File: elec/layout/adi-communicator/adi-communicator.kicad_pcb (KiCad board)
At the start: 2 copper layers, 225.7 x 100.8 mm, 0 parts

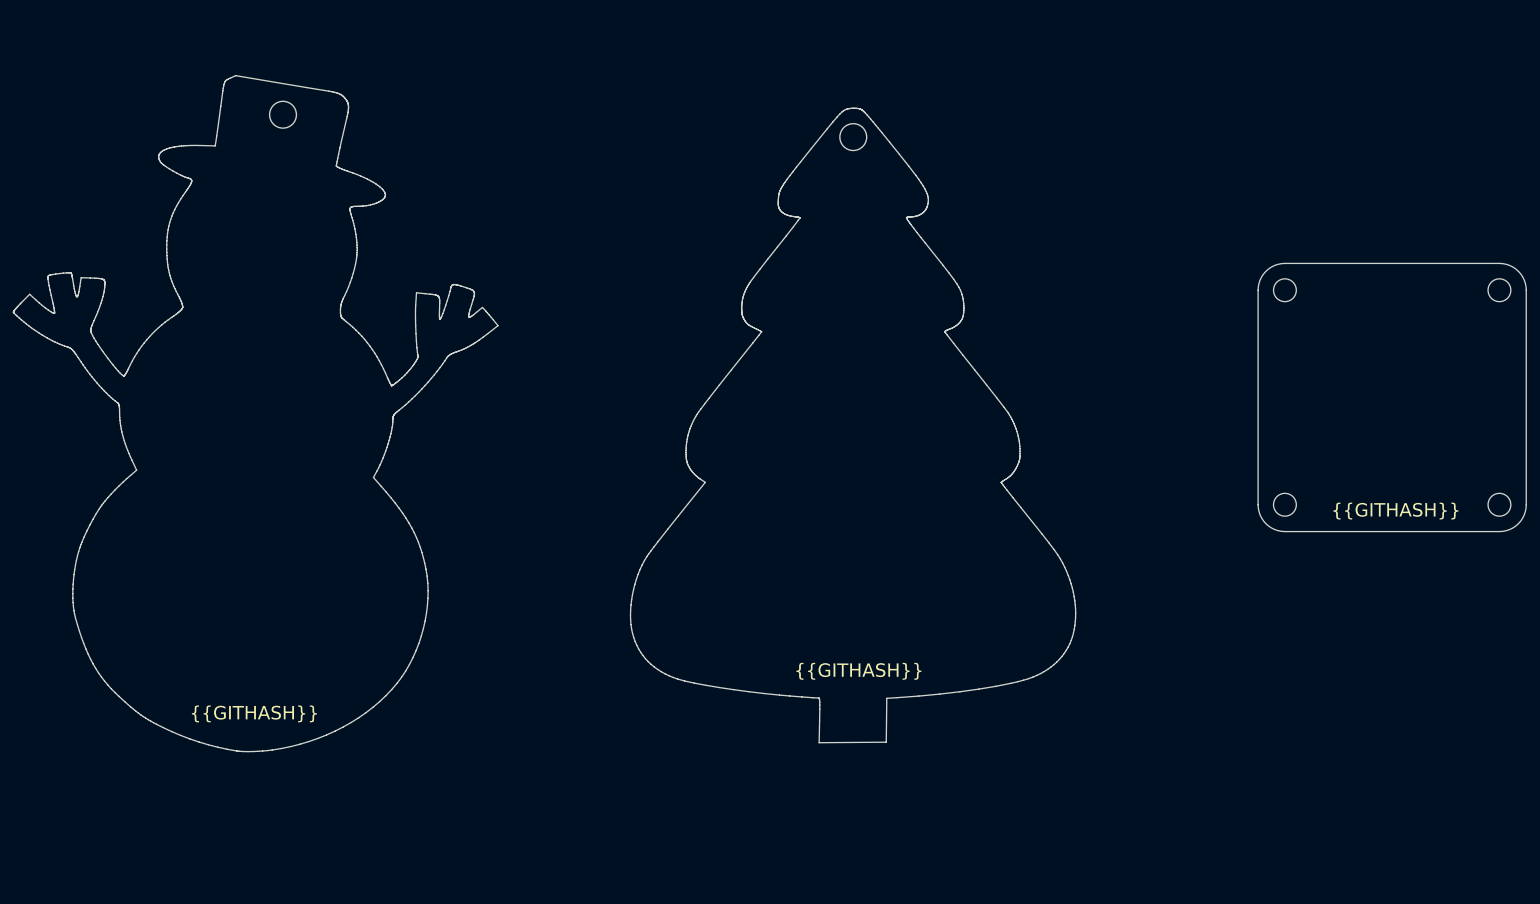
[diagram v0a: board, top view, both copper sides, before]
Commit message: Remove xmas tree from layout
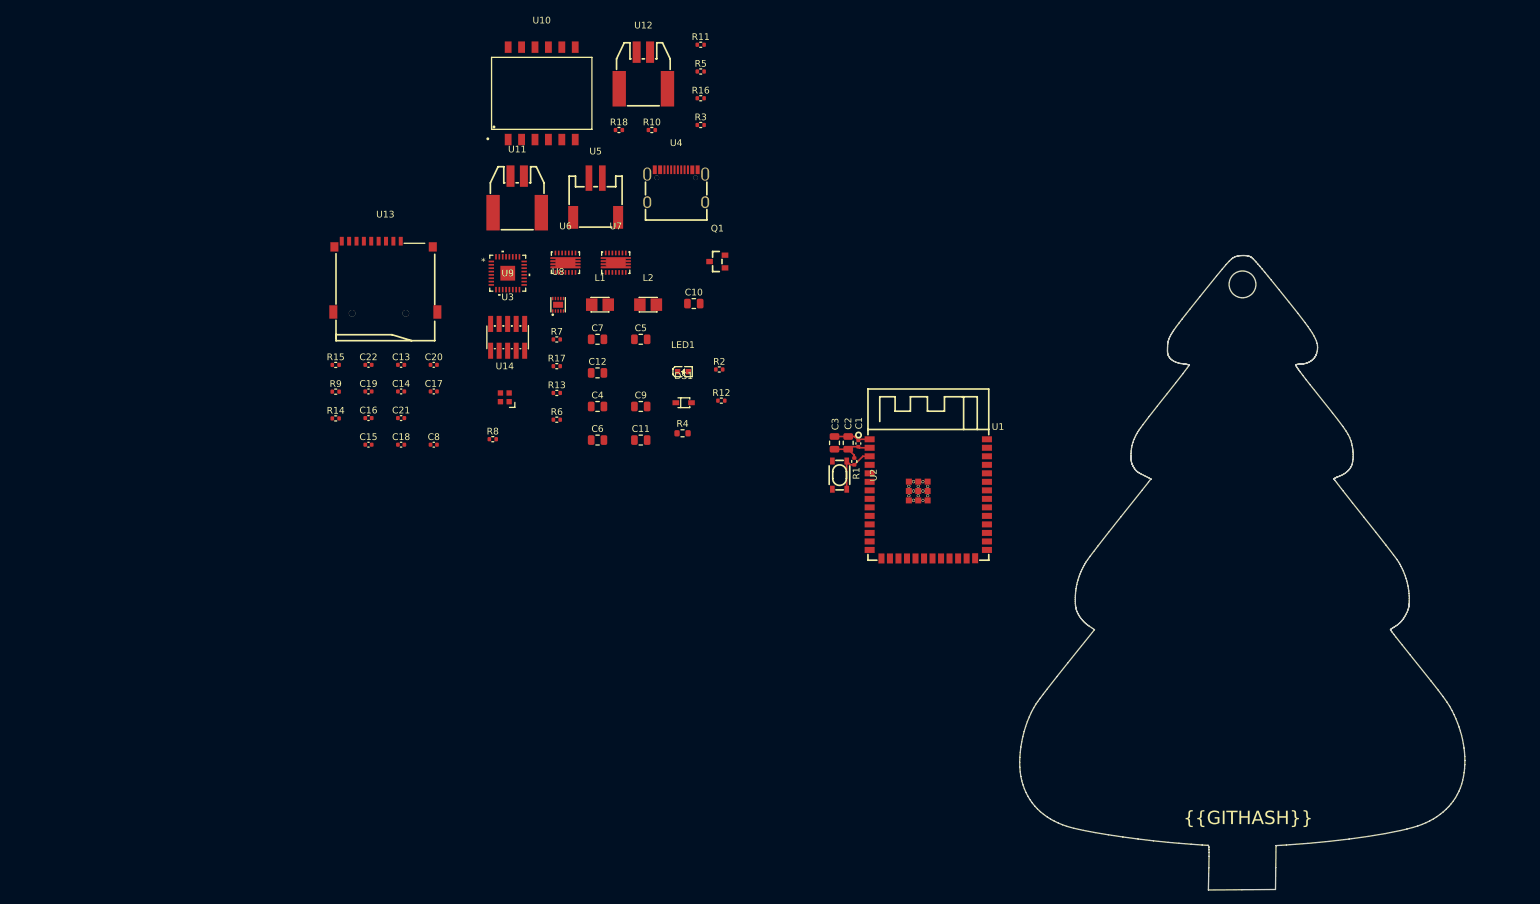
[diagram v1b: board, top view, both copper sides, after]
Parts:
- added C1: 16V 100nF X7R ±10% 0402 Multilayer Ceramic Capacitors MLCC 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, lib:C0402, F.Cu at (162.0, 104.7)
- added C10: 25V 10uF X5R ±10% 0805 Multilayer Ceramic Capacitors MLCC -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, lib:C0805, F.Cu at (137.4, 83.8)
- added C11: 25V 10uF X5R ±10% 0805 Multilayer Ceramic Capacitors MLCC -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, lib:C0805, F.Cu at (129.5, 104.1)
- added C12: 25V 10uF X5R ±10% 0805 Multilayer Ceramic Capacitors MLCC -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, lib:C0805, F.Cu at (123.1, 94.1)
- added C13: 16V 100nF X7R ±10% 0402 Multilayer Ceramic Capacitors MLCC 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, lib:C0402, F.Cu at (93.8, 92.9)
- added C14: 25V 1uF X5R ±10% 0402 Multilayer Ceramic Capacitors MLCC - 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, lib:C0402, F.Cu at (93.8, 96.9)
- added C15: 25V 1uF X5R ±10% 0402 Multilayer Ceramic Capacitors MLCC - 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, lib:C0402, F.Cu at (88.9, 104.8)
- added C16: 16V 100nF X7R ±10% 0402 Multilayer Ceramic Capacitors MLCC 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, lib:C0402, F.Cu at (88.9, 100.9)
- added C17: 16V 100nF X7R ±10% 0402 Multilayer Ceramic Capacitors MLCC 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, lib:C0402, F.Cu at (98.7, 96.9)
- added C18: 16V 100nF X7R ±10% 0402 Multilayer Ceramic Capacitors MLCC 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, lib:C0402, F.Cu at (93.8, 104.8)
- added C19: 16V 100nF X7R ±10% 0402 Multilayer Ceramic Capacitors MLCC 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, lib:C0402, F.Cu at (88.9, 96.9)
- added C2: 25V 10uF X5R ±10% 0805 Multilayer Ceramic Capacitors MLCC -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, lib:C0805, F.Cu at (160.5, 104.6)
- added C20: 16V 100nF X7R ±10% 0402 Multilayer Ceramic Capacitors MLCC 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, lib:C0402, F.Cu at (98.7, 92.9)
- added C21: 16V 100nF X7R ±10% 0402 Multilayer Ceramic Capacitors MLCC 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, lib:C0402, F.Cu at (93.8, 100.9)
- added C22: 16V 100nF X7R ±10% 0402 Multilayer Ceramic Capacitors MLCC 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, lib:C0402, F.Cu at (88.9, 92.9)
- added C3: 25V 10uF X5R ±10% 0805 Multilayer Ceramic Capacitors MLCC -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, lib:C0805, F.Cu at (158.4, 104.6)
- added C4: 25V 10uF X5R ±10% 0805 Multilayer Ceramic Capacitors MLCC -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, lib:C0805, F.Cu at (123.1, 99.1)
- added C5: 25V 10uF X5R ±10% 0805 Multilayer Ceramic Capacitors MLCC -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, lib:C0805, F.Cu at (129.5, 89.1)
- added C6: 25V 10uF X5R ±10% 0805 Multilayer Ceramic Capacitors MLCC -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, lib:C0805, F.Cu at (123.1, 104.1)
- added C7: 25V 10uF X5R ±10% 0805 Multilayer Ceramic Capacitors MLCC -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, lib:C0805, F.Cu at (123.1, 89.1)
- added C8: 16V 100nF X7R ±10% 0402 Multilayer Ceramic Capacitors MLCC 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, lib:C0402, F.Cu at (98.7, 104.8)
- added C9: 25V 10uF X5R ±10% 0805 Multilayer Ceramic Capacitors MLCC -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, lib:C0805, F.Cu at (129.5, 99.1)
- added DS1: , lib:SOD-323_L1.8-W1.3-LS2.5-RD, F.Cu at (135.9, 98.6)
- added L1: , lib:IND-SMD_L2.5-W2.0_WPN252012H, F.Cu at (123.4, 83.9)
- added L2: , lib:IND-SMD_L2.5-W2.0_WPN252012H, F.Cu at (130.6, 83.9)
- added LED1: , lib:LED0603-RD, F.Cu at (135.8, 93.9)
- added Q1: , lib:SOT-23_L2.9-W1.3-P1.90-LS2.4-BR, F.Cu at (140.9, 77.5)
- added R1: 62.5mW Thick Film Resistors 50V ±100ppm/℃ ±1% 10kΩ 0402 Chi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, lib:R0402, F.Cu at (161.4, 107.3)
- added R10: 62.5mW Thick Film Resistors 50V ±100ppm/℃ ±1% 1MΩ 0402 Chip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, lib:R0402, F.Cu at (131.2, 57.9)
- added R11: 62.5mW Thick Film Resistors 50V ±100ppm/℃ ±1% 330Ω 0402 Chi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, lib:R0402, F.Cu at (138.5, 45.2)
- added R12: 62.5mW Thick Film Resistors 75V ±1% ±100ppm/℃ 576Ω 0402 Chi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, lib:R0402, F.Cu at (141.6, 98.3)
- added R13: 0Ω, lib:R0402, F.Cu at (117.0, 97.1)
- added R14: 0Ω, lib:R0402, F.Cu at (84.0, 100.9)
- added R15: 0Ω, lib:R0402, F.Cu at (84.0, 92.9)
- added R16: 0Ω, lib:R0402, F.Cu at (138.5, 53.1)
- added R17: 0Ω, lib:R0402, F.Cu at (117.0, 93.1)
- added R18: 0Ω, lib:R0402, F.Cu at (126.3, 57.9)
- added R2: 62.5mW Thick Film Resistors 50V ±100ppm/℃ ±1% 4.7kΩ 0402 Ch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, lib:R0402, F.Cu at (141.2, 93.6)
- added R3: 62.5mW Thick Film Resistors 50V ±100ppm/℃ ±1% 4.7kΩ 0402 Ch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, lib:R0402, F.Cu at (138.5, 57.1)
- added R4: 100mW Thick Film Resistors 75V ±100ppm/℃ ±1% 10kΩ 0603 Chip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, lib:R0603, F.Cu at (135.8, 103.1)
- added R5: 62.5mW Thick Film Resistors 50V ±100ppm/℃ ±1% 25.5kΩ 0402 C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, lib:R0402, F.Cu at (138.5, 49.2)
- added R6: 62.5mW Thick Film Resistors ±100ppm/℃ ±1% 2.8kΩ 0402 Chip R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, lib:R0402, F.Cu at (117.0, 101.1)
- added R7: 62.5mW Thick Film Resistors 50V ±100ppm/℃ ±1% 1MΩ 0402 Chip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, lib:R0402, F.Cu at (117.0, 89.1)
- added R8: 62.5mW Thick Film Resistors 50V ±100ppm/℃ ±1% 23.7kΩ 0402 C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, lib:R0402, F.Cu at (107.5, 104.0)
- added R9: 62.5mW Thick Film Resistors 50V ±100ppm/℃ ±1% 4.3kΩ 0402 Ch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, lib:R0402, F.Cu at (84.0, 96.9)
- added U1: , lib:WIRELM-SMD_ESP32-S3-WROOM-1, F.Cu at (172.4, 112.9)
- added U10: , lib:SMD-12_L14.8-W11.7-P2.00-LS14.7, F.Cu at (114.8, 52.4)
- added U11: , lib:CONN-SMD_2P-P2.00_MOLEX_5023520201, F.Cu at (111.1, 67.5)
- added U12: , lib:CONN-SMD_2P-P2.00_MOLEX_5023520201, F.Cu at (129.9, 49.0)
- added U13: , lib:TF-SMD_TF-01A, F.Cu at (91.4, 79.8)
- added U14: , lib:LED-SMD_4P-L2.0-W2.0-BR, F.Cu at (109.2, 97.8)
- added U2: , lib:KEY-SMD_4P-L4.2-W3.2-P2.20-LS4.6, F.Cu at (159.2, 109.4)
- added U3: , lib:HDR-SMD_10P-P1.27-V-M-R2-C5-LS5.3, F.Cu at (109.7, 88.8)
- added U4: , lib:USB-C-SMD_KH-TYPE-C-16P, F.Cu at (134.8, 66.2)
- added U5: , lib:CONN-SMD_P2.00_S2B-PH-SM4-TB-LF-SN, F.Cu at (122.8, 68.0)
- added U6: , lib:VSON-14_L4.0-W3.0-P0.50-BL-EP_TI_DSJ, F.Cu at (118.3, 77.7)
- added U7: , lib:VSON-14_L4.0-W3.0-P0.50-BL-EP_TI_DSJ, F.Cu at (125.8, 77.7)
- added U8: , lib:WSON-10_L2.0-W2.0-P0.40-BL-EP, F.Cu at (117.2, 84.0)
- added U9: , lib:05-08-7057_ADI, F.Cu at (109.7, 79.3)
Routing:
- net en: track 0.00 -> 8.40 mm
- net uc.ic-vcc: track 0.00 -> 7.15 mm
- net uc.ic-gnd: track 0.00 -> 5.54 mm
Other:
- board size 225.7 x 100.8 mm -> 66.4 x 94.6 mm

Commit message: Placement and zones done. Small routing largely complete
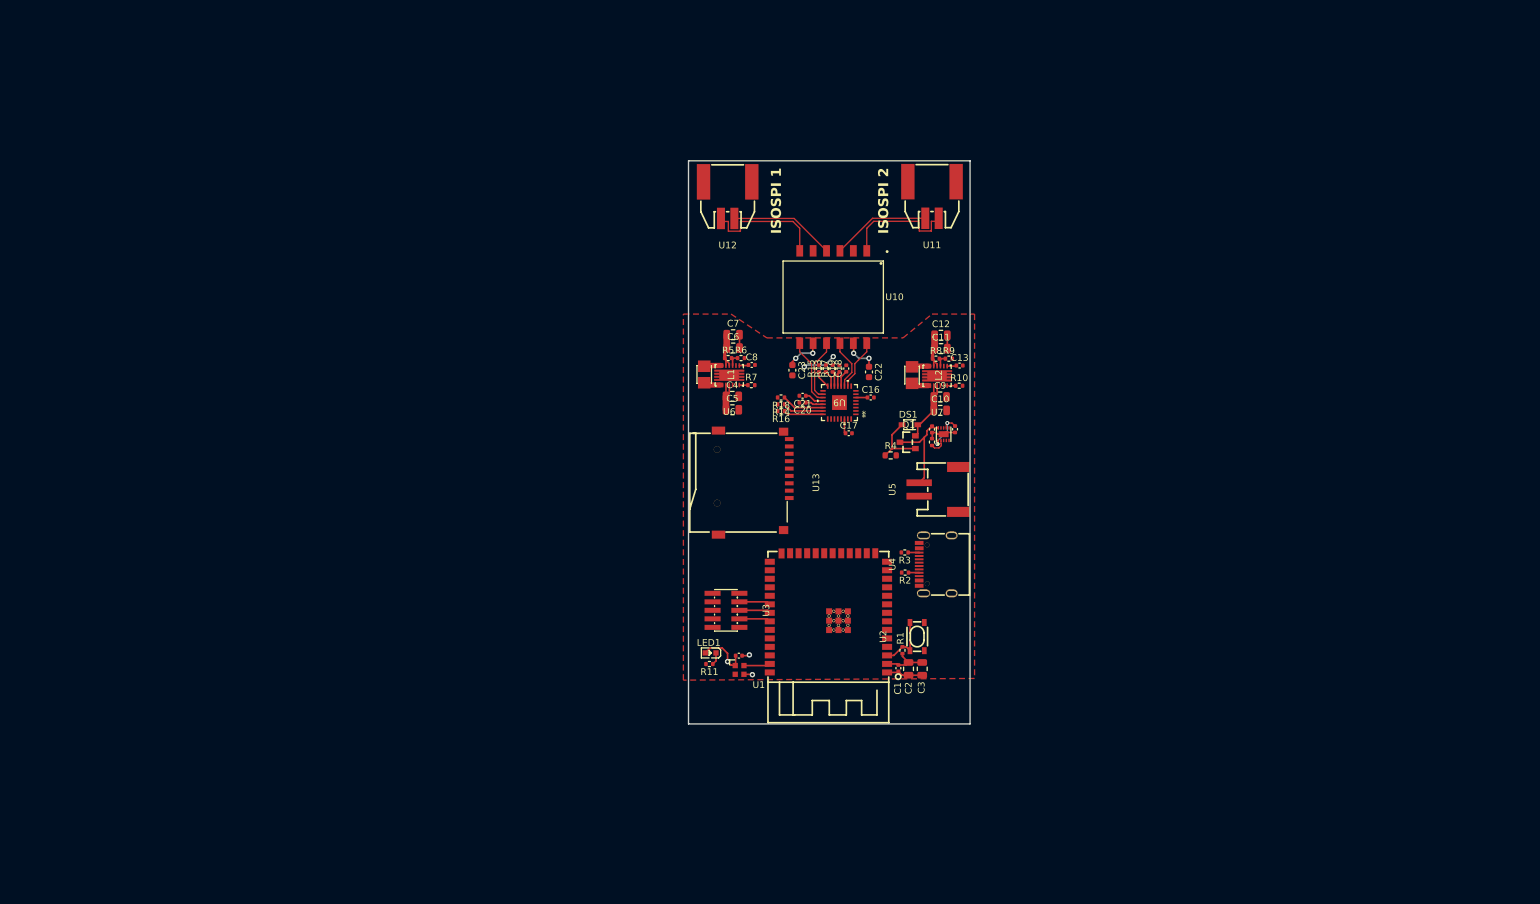
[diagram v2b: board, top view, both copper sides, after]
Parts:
- added C22: 50V 10nF X7R ±10% 0603 Multilayer Ceramic Capacitors MLCC -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, lib:C0603, F.Cu at (163.6, 94.0)
- added C23: 50V 10nF X7R ±10% 0603 Multilayer Ceramic Capacitors MLCC -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, lib:C0603, F.Cu at (152.1, 93.7)
- moved R11 92.4 mm to (139.8, 137.5), turned to 180 degrees
- moved R9 91.6 mm to (175.5, 92.0)
- moved C15 84.1 mm to (173.0, 102.5), turned to -90 degrees
- moved C13 83.3 mm to (177.1, 93.0)
- moved C14 82.8 mm to (176.4, 102.5), turned to -90 degrees
- moved C16 75.0 mm to (163.8, 97.8)
- moved R15 72.1 mm to (156.1, 93.5), turned to 90 degrees
- moved R3 70.7 mm to (168.9, 120.9), turned to 180 degrees
- moved C19 70.3 mm to (159.2, 93.5), turned to 90 degrees
- moved C24 70.2 mm to (144.2, 136.3)
- moved U4 68.4 mm to (173.5, 122.7), turned to 90 degrees
- moved C18 67.4 mm to (160.2, 93.5), turned to 90 degrees
- moved R8 67.2 mm to (173.6, 92.0)
- moved U5 67.2 mm to (174.0, 111.5), turned to 90 degrees
- moved R14 66.5 mm to (150.5, 98.8), turned to 180 degrees
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- renumbered C22 to C24
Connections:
- C10 pad 2: uc-gnd-1 -> uc.ic-gnd
- C11 pad 1: _3v3_reg-vcc -> uc.ic-vcc
- C11 pad 2: uc-gnd-1 -> uc.ic-gnd
- C12 pad 1: _3v3_reg-vcc -> uc.ic-vcc
- C12 pad 2: uc-gnd-1 -> uc.ic-gnd
- C13 pad 2: uc-gnd-1 -> uc.ic-gnd
- C14 pad 2: uc-gnd-1 -> uc.ic-gnd
- C15 pad 2: uc-gnd-1 -> uc.ic-gnd
- C16 pad 1: _nic._ic-vcc -> uc.ic-vcc
- C16 pad 2: _nic-gnd -> uc.ic-gnd
- C17 pad 1: _nic._ic-vcc -> uc.ic-vcc
- C17 pad 2: _nic-gnd -> uc.ic-gnd
- C18 pad 1: _nic._ic-vcc -> _5v_reg-vcc
- C18 pad 2: _nic-gnd -> uc.ic-gnd
- C19 pad 1: _nic._ic-vcc -> _5v_reg-vcc
- C19 pad 2: _nic-gnd -> uc.ic-gnd
- C20 pad 1: _nic._ic-vcc -> _5v_reg-vcc
- C20 pad 2: _nic-gnd -> uc.ic-gnd
- C21 pad 1: _nic._ic-vcc -> _5v_reg-vcc
- C21 pad 2: _nic-gnd -> uc.ic-gnd
- C24 pad 1: _led.ic-vcc -> uc.ic-vcc
- C24 pad 2: _led.ic-gnd -> uc.ic-gnd
- C4 pad 2: uc-gnd-1 -> uc.ic-gnd
- C5 pad 2: uc-gnd-1 -> uc.ic-gnd
- C6 pad 2: uc-gnd-1 -> uc.ic-gnd
- C7 pad 2: uc-gnd-1 -> uc.ic-gnd
- C8 pad 2: uc-gnd-1 -> uc.ic-gnd
- C9 pad 2: uc-gnd-1 -> uc.ic-gnd
- LED1 pad 2: _3v3_reg-vcc -> uc.ic-vcc
- R10 pad 2: uc-gnd-1 -> uc.ic-gnd
- R11 pad 2: uc-gnd-1 -> uc.ic-gnd
- R12 pad 2: uc-gnd-1 -> uc.ic-gnd
- R13 pad 2: _nic-gnd -> uc.ic-gnd
- R14 pad 2: _nic-gnd -> uc.ic-gnd
- R15 pad 1: rto -> xcvrmd
- R15 pad 2: _nic-gnd -> uc.ic-gnd
- R16 pad 1: rto2 -> xcvrmd2
- R16 pad 2: _nic-gnd -> uc.ic-gnd
- R17 pad 1: rto -> phapol
- R17 pad 2: _nic-gnd -> uc.ic-gnd
- R18 pad 1: rto2 -> phapol2
- R18 pad 2: _nic-gnd -> uc.ic-gnd
- R2 pad 2: uc-gnd-1 -> uc.ic-gnd
- R3 pad 2: uc-gnd-1 -> uc.ic-gnd
- R4 pad 2: uc-gnd-1 -> uc.ic-gnd
- R6 pad 2: uc-gnd-1 -> uc.ic-gnd
- R7 pad 2: uc-gnd-1 -> uc.ic-gnd
- R8 pad 1: _3v3_reg-vcc -> uc.ic-vcc
- R9 pad 2: uc-gnd-1 -> uc.ic-gnd
- U1 pad 15: io3 -> uc.ic-sck-1
- U1 pad 16: io46 -> uc.ic-miso-1
- U1 pad 17: io9 -> uc.ic-mosi-1
- U1 pad 19: uc.ic-mosi-1 -> uc.ic-mosi
- U1 pad 20: uc.ic-sck-1 -> uc.ic-sck
- U1 pad 21: uc.ic-miso-1 -> uc.ic-miso
- U1 pad 28: uc.ic-miso -> io35
- U1 pad 29: uc.ic-mosi -> io36
- U1 pad 30: uc.ic-sck -> io37
- U10 pad 1: _iso_transformer-p -> isospi_hv_1-
- U10 pad 10: _nic._ic-n -> isospi_safe_1+
- U10 pad 12: _nic._ic-p -> isospi_safe_1-
- U10 pad 3: _iso_transformer-n -> isospi_hv_1+
- U10 pad 4: _iso_transformer-p-1 -> isospi_hv_2-
- U10 pad 6: _iso_transformer-n-1 -> isospi_hv_2+
- U10 pad 7: _nic._ic-n-1 -> isospi_safe_2+
- U10 pad 9: _nic._ic-p-1 -> isospi_safe_2-
- U11 pad 1: _iso_transformer-p -> isospi_hv_1+
- U11 pad 2: _iso_transformer-n -> isospi_hv_1-
- U12 pad 1: _iso_transformer-p-1 -> isospi_hv_2+
- U12 pad 2: _iso_transformer-n-1 -> isospi_hv_2-
- U13 pad 10: uc-gnd-1 -> uc.ic-gnd
- U13 pad 11: uc-gnd-1 -> uc.ic-gnd
- U13 pad 12: uc-gnd-1 -> uc.ic-gnd
- U13 pad 13: uc-gnd-1 -> uc.ic-gnd
- U13 pad 3: uc.ic-mosi-1 -> uc.ic-mosi
- U13 pad 4: _3v3_reg-vcc -> uc.ic-vcc
- U13 pad 5: uc.ic-sck-1 -> uc.ic-sck
- U13 pad 6: uc-gnd-1 -> uc.ic-gnd
- U13 pad 7: uc.ic-miso-1 -> uc.ic-miso
- U14 pad 1: _led.ic-vcc -> uc.ic-vcc
- U14 pad 2: _led.ic-vcc-1 -> _led.ic-vcc
- U14 pad 3: _led.ic-gnd -> uc.ic-gnd
- U14 pad 4: io21 -> io1
- U4 pad 1: uc-gnd-1 -> uc.ic-gnd
- U4 pad 2: uc-gnd-1 -> uc.ic-gnd
- U4 pad 3: uc-gnd-1 -> uc.ic-gnd
- U4 pad 4: uc-gnd-1 -> uc.ic-gnd
- U4 pad A1: uc-gnd-1 -> uc.ic-gnd
- U4 pad A12: uc-gnd-1 -> uc.ic-gnd
- U4 pad B1: uc-gnd-1 -> uc.ic-gnd
- U4 pad B12: uc-gnd-1 -> uc.ic-gnd
- U5 pad 1: uc-gnd-1 -> uc.ic-gnd
- U6 pad 13: uc-gnd-1 -> uc.ic-gnd
- U6 pad 15: uc-gnd-1 -> uc.ic-gnd
- U6 pad 2: uc-gnd-1 -> uc.ic-gnd
- U7 pad 13: uc-gnd-1 -> uc.ic-gnd
- U7 pad 15: uc-gnd-1 -> uc.ic-gnd
- U7 pad 2: uc-gnd-1 -> uc.ic-gnd
- U7 pad 4: _3v3_reg-vcc -> uc.ic-vcc
- U7 pad 5: _3v3_reg-vcc -> uc.ic-vcc
- U8 pad 11: uc-gnd-1 -> uc.ic-gnd
- U8 pad 3: uc-gnd-1 -> uc.ic-gnd
- U9 pad 10: _nic._ic-n -> isospi_safe_1-
- U9 pad 11: _nic._ic-p -> isospi_safe_1+
- U9 pad 12: vdd -> _5v_reg-vcc
- U9 pad 13: vdd -> _5v_reg-vcc
- U9 pad 17: _nic-gnd -> uc.ic-gnd
- U9 pad 18: _nic._ic-n-1 -> isospi_safe_2-
- U9 pad 19: _nic._ic-p-1 -> isospi_safe_2+
- U9 pad 2: uc.ic-mosi -> uc.ic-mosi-1
- U9 pad 20: vdd -> _5v_reg-vcc
- U9 pad 21: vdd -> _5v_reg-vcc
- U9 pad 26: uc.ic-mosi -> uc.ic-mosi-1
- U9 pad 27: uc.ic-miso -> uc.ic-miso-1
- U9 pad 28: uc.ic-sck -> uc.ic-sck-1
- U9 pad 29: io45 -> io18
- U9 pad 3: uc.ic-miso -> uc.ic-miso-1
- U9 pad 30: _nic._ic-vcc -> uc.ic-vcc
- U9 pad 33: _nic-gnd -> uc.ic-gnd
- U9 pad 4: uc.ic-sck -> uc.ic-sck-1
- U9 pad 5: io38 -> io8
- U9 pad 6: _nic._ic-vcc -> uc.ic-vcc
- U9 pad 9: _nic-gnd -> uc.ic-gnd
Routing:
- net isospi_hv_2+: track 0.00 -> 18.6 mm
- net uc.ic-vcc: track 7.15 -> 25.4 mm, vias 0 -> 1
- net isospi_hv_1-: track 0.00 -> 17.6 mm
- net _5v_reg-vcc: track 0.00 -> 16.5 mm
- net power_prio-vcc: track 0.00 -> 16.4 mm
- net uc.ic-gnd: track 5.54 -> 21.4 mm, vias 0 -> 4
- net isospi_hv_2-: track 0.00 -> 15.8 mm
- net usb_conn-vcc: track 0.00 -> 15.6 mm, vias 0 -> 2
- net isospi_hv_1+: track 0.00 -> 14.7 mm
- net battery_conn-vcc: track 0.00 -> 14.3 mm
- net isospi_safe_2+: track 0.00 -> 10.0 mm
- net isospi_safe_2-: track 0.00 -> 9.32 mm
- net isospi_safe_1-: track 0.00 -> 7.60 mm
- net isospi_safe_1+: track 0.00 -> 7.59 mm
- net phapol2: track 0.00 -> 6.38 mm
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- added copper zone on F.Cu, net uc.ic-gnd
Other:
- board size 66.4 x 94.6 mm -> 42 x 84 mm
- copper layers 2 -> 4
- board text added: "ISOSPI 1"
- board text added: "ISOSPI 2"
- board text removed: "{{GITHASH}}"

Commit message: Layout communicator
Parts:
- added REF**: MountingHole_3.2mm_M3_DIN965_Pad, MountingHole:MountingHole_3.2mm_M3_DIN965_Pad, F.Cu at (158.2, 67.1)
- added REF**: MountingHole_3.2mm_M3_DIN965_Pad, MountingHole:MountingHole_3.2mm_M3_DIN965_Pad, F.Cu at (140.0, 143.0)
- added REF**: MountingHole_3.2mm_M3_DIN965_Pad, MountingHole:MountingHole_3.2mm_M3_DIN965_Pad, F.Cu at (175.3, 143.0)
- added REF**: PinHeader_1x04_P2.54mm_Vertical, Connector_PinHeader_2.54mm:PinHeader_1x04_P2.54mm_Vertical, F.Cu at (138.4, 122.2)
- added REF**: PinHeader_1x04_P2.54mm_Vertical, Connector_PinHeader_2.54mm:PinHeader_1x04_P2.54mm_Vertical, B.Cu at (176.0, 137.4)
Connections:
- net dm renamed usb-
- net dp renamed usb+
- U9 pad 29: io18 -> io8
- U9 pad 5: io8 -> io18
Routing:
- net uc.ic-sck-1: track 0.00 -> 35.6 mm, vias 0 -> 2
- net uc.ic-miso-1: track 0.00 -> 35.6 mm, vias 0 -> 2
- net usb_conn-vcc: track 15.6 -> 51.1 mm, vias 2 -> 4
- net io18: track 0.00 -> 34.7 mm, vias 0 -> 2
- net power_prio-vcc: track 16.4 -> 47.7 mm, vias 0 -> 2
- net io8: track 0.00 -> 30.2 mm, vias 0 -> 2
- net uc.ic-mosi-1: track 0.00 -> 26.3 mm
- net _5v_reg-vcc: track 16.5 -> 38.3 mm
- net uc.ic-miso: track 0.00 -> 19.8 mm
- net uc.ic-gnd: track 21.4 -> 40.9 mm, vias 4 -> 11
- net uc.ic-sck: track 0.00 -> 17.8 mm
- net uc.ic-mosi: track 0.00 -> 16.1 mm
- net cs: track 0.00 -> 15.6 mm
- net _5v_reg.ic-vina: track 1.41 -> 16.6 mm
- net _3v3_reg.ic-vina: track 1.41 -> 16.0 mm, vias 0 -> 2
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- added copper zone on B.Cu, net uc.ic-gnd
- added copper zone on In1.Cu, net uc.ic-gnd
- added copper zone on In2.Cu, net uc.ic-vcc
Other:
- outline, holes or cut-outs redrawn
- board text added: "1 GND 2 io15 3 io16 4 io17"
- board text added: "1 GND 2 io36 3 io35 4 io0"
- board text added: "1500V MAX"
- board text added: "Designed by Matt Wildoer"
- board text added: "{{GITHASH}}"
